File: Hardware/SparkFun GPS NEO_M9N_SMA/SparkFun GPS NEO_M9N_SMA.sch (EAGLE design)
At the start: 52 parts, among them J2 Qwiic Right Angle, J4 Qwiic Right Angle, U1 U-BLOX_NEO-M9N, U2 3.3V

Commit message: Changes to female SMD, SMA connector
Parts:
- E1: value ANTENNA-GROUNDEDEDGE_RPSMA_SMD -> ANTENNA-GROUNDEDEDGE_SMA_SMD; device SparkFun-RF:ANTENNA-GROUNDEDEDGE_RPSMA_SMD -> SparkFun-RF:ANTENNA-GROUNDEDEDGE_SMA_SMD
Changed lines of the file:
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@@
 <part name="R16" library="SparkFun-Resistors" deviceset="10KOHM" device="-0402-1/16W-1%" value="10k"/>
 <part name="SUPPLY12" library="SparkFun-PowerSymbols" deviceset="3.3V" device=""/>
-<part name="E1" library="SparkFun-RF" deviceset="ANTENNA-GROUNDED" device="EDGE_RPSMA_SMD"/>
+<part name="E1" library="SparkFun-RF" deviceset="ANTENNA-GROUNDED" device="EDGE_SMA_SMD" value="ANTENNA-GROUNDEDEDGE_SMA_SMD"/>
 <part name="FB1" library="SparkFun-Coils" deviceset="FERRITE_BEAD-120_OHM" device="-0402"/>
 <part name="C1" library="SparkFun-Capacitors" deviceset="47PF" device="-0402-25V-5%-X7R" value="47pF"/>

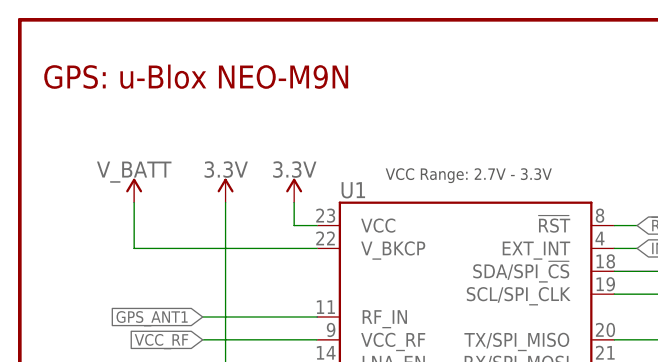
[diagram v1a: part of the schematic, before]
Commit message: Fixes "u-blox" typos in schematic
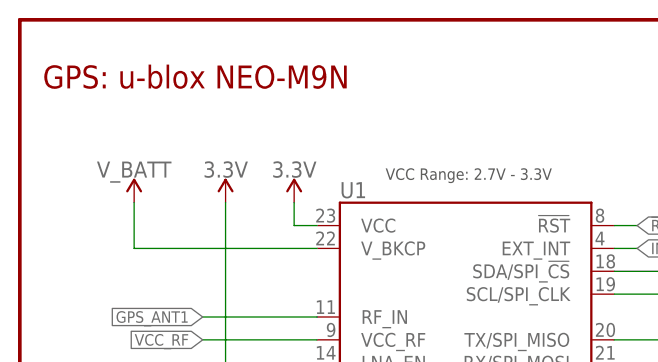
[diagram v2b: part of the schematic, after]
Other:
- note added: "GPS: u-blox NEO-M9N"
- note removed: "GPS: u-Blox NEO-M9N"
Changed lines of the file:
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@@
 <?xml version="1.0" encoding="utf-8"?>
 <!DOCTYPE eagle SYSTEM "eagle.dtd">
-<eagle version="9.5.2">
+<eagle version="9.6.2">
 <drawing>
 <settings>
@@
 <text x="2.54" y="99.06" size="2.54" layer="94" font="vector">LEDs and Jumpers</text>
 <text x="149.86" y="116.84" size="2.54" layer="94" font="vector">Hot Start Battery</text>
-<text x="2.54" y="177.8" size="2.54" layer="94" font="vector">GPS: u-Blox NEO-M9N </text>
+<text x="2.54" y="177.8" size="2.54" layer="94" font="vector">GPS: u-blox NEO-M9N </text>
 <wire x1="73.66" y1="106.68" x2="73.66" y2="0" width="0.1524" layer="97" style="shortdash"/>
 <text x="198.12" y="116.84" size="2.54" layer="94" font="vector">SMA Connector</text>
